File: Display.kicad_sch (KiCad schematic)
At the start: 10 parts, among them J3 541043431, U6 1SS383TE85L_F

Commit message: Create PCB
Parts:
- removed C27: 1uF, Capacitor_SMD:C_0603_1608Metric, symbol Device:C_Small
- added C28: 1uF, Capacitor_SMD:C_0603_1608Metric, symbol Device:C_Small
- added R17: 100K, Resistor_SMD:R_0402_1005Metric, symbol Device:R_Small
- C27: renamed from C26; DigiKey_Part_Number (none) -> 311-1445-1-ND; Manufacturer_Part_Number (none) -> CC0603KRX5R8BB105; Price (none) -> €0.95
- C29: renamed from C28; DigiKey_Part_Number (none) -> 311-1445-1-ND; Manufacturer_Part_Number (none) -> CC0603KRX5R8BB105; Price (none) -> €0.95
- C30: renamed from C29; DigiKey_Part_Number (none) -> 311-1445-1-ND; Manufacturer_Part_Number (none) -> CC0603KRX5R8BB105; Price (none) -> €0.95
- C31: renamed from C30; footprint Capacitor_SMD:C_0603_1608Metric -> Capacitor_SMD:C_0805_2012Metric; DigiKey_Part_Number (none) -> 1276-1244-1-ND; Manufacturer_Part_Number (none) -> CL21A475KAQNNNE; Price (none) -> €0.30
- C32: renamed from C31; footprint Capacitor_SMD:C_0603_1608Metric -> Capacitor_SMD:C_0805_2012Metric; DigiKey_Part_Number (none) -> 1276-1244-1-ND; Manufacturer_Part_Number (none) -> CL21A475KAQNNNE; Price (none) -> €0.30
- J3: DigiKey_Part_Number (none) -> 900-0541043431CT-ND; Manufacturer_Part_Number (none) -> 0541043431; Price (none) -> €2.66
- R18: renamed from R16; value 49.9 -> 100K; footprint Resistor_SMD:R_0603_1608Metric -> Resistor_SMD:R_0402_1005Metric; DigiKey_Part_Number (none) -> 311-100KLRCT-ND; Manufacturer_Part_Number (none) -> RC0402FR-07100KL; Price (none) -> €0.40
- R19: renamed from R17; footprint Resistor_SMD:R_0603_1608Metric -> Resistor_SMD:R_0402_1005Metric; DigiKey_Part_Number (none) -> YAG5649CT-ND; Manufacturer_Part_Number (none) -> AC0402FR-071M2L; Price (none) -> €0.10
- U7: renamed from U6; DigiKey_Part_Number (none) -> 1SS383(TE85LF)CT-ND; Manufacturer_Part_Number (none) -> 1SS383(TE85L,F); Price (none) -> €0.27
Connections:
- net 3V3: now also C27.1, C28.1; no longer C27.2
- net GND: now also C27.2, C28.2; no longer C27.1
- net at J3.7, R18.1: now also R17.1
- net at R18.2, U7.2: now also R17.2
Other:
- moved on the sheet: C27, R18, U7

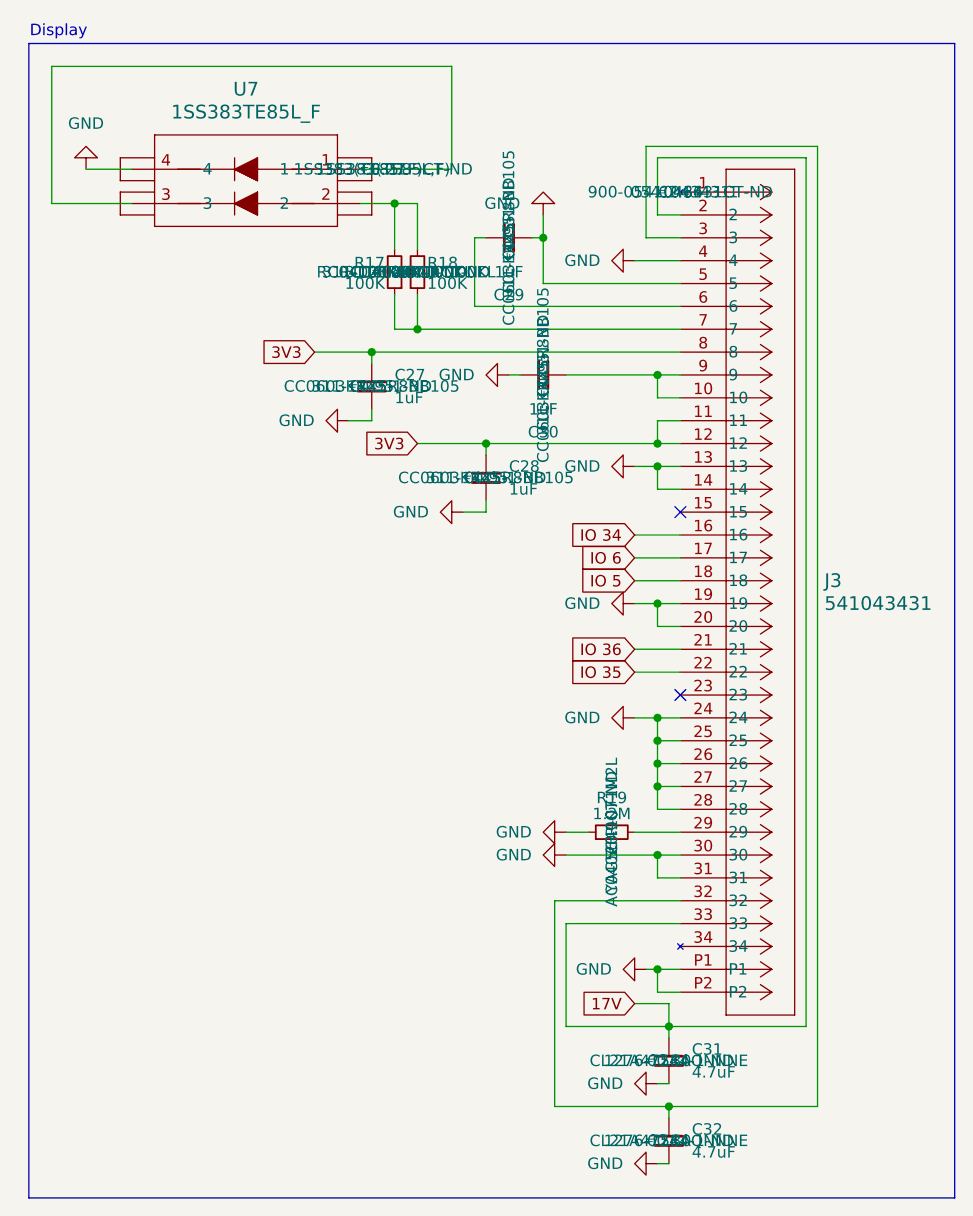
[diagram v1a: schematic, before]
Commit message: Fix minor design mistakes
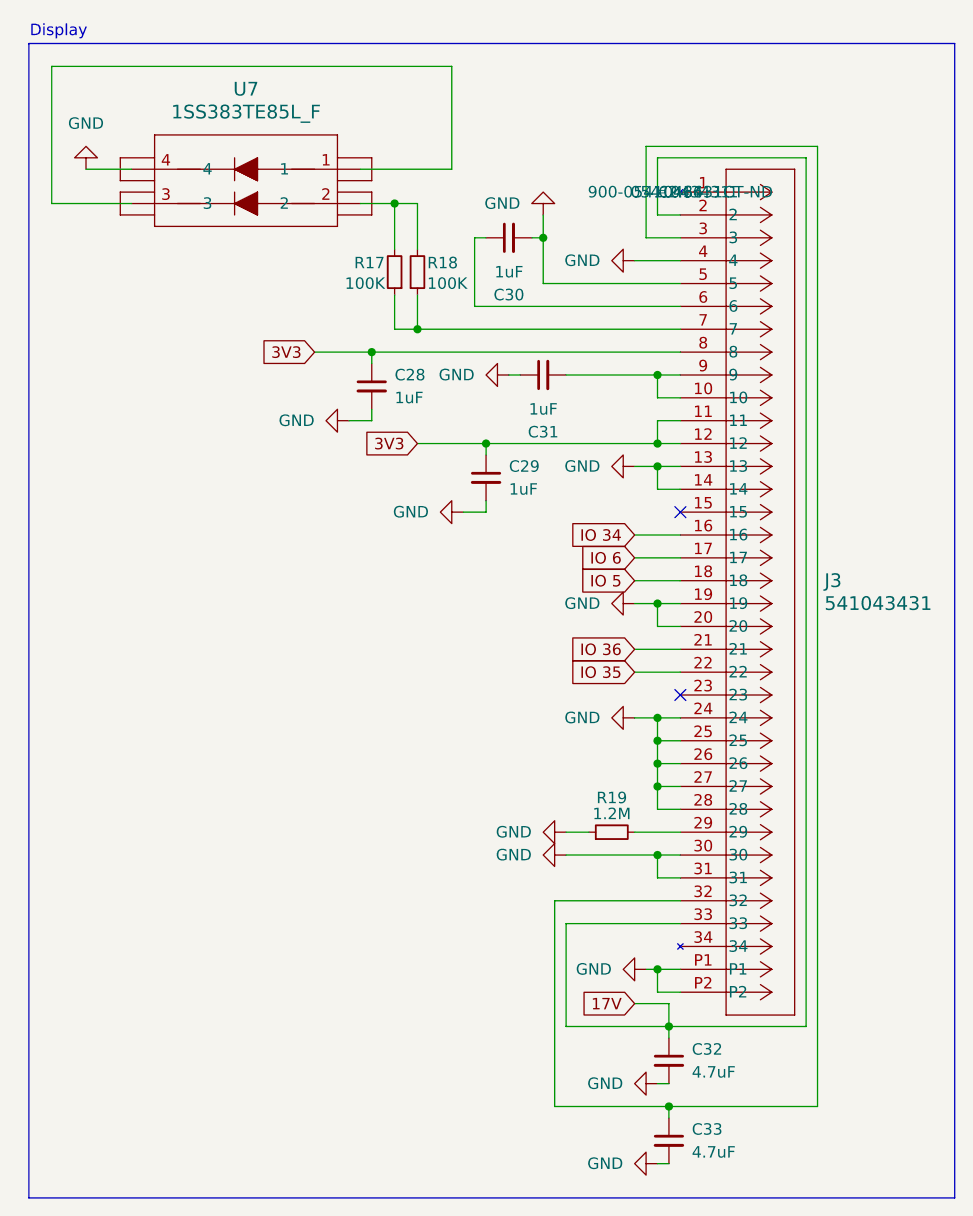
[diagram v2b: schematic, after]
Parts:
- renumbered C27 to C28, C28 to C29, C29 to C30, C30 to C31, C31 to C32, C32 to C33
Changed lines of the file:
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@@
 		(dnp no)
 		(fields_autoplaced yes)
-		(property "Reference" "#PWR032"
+		(property "Reference" "#PWR034"
 			(at 55.88 67.31 0)
 			(effects
@@
 			(project "RFID_Device"
 				(path "/f4733a35-9ae9-40ca-bc69-86dc96557334/b995fd20-39e2-4c72-9eca-13ccf0f092d3"
-					(reference "#PWR032")
+					(reference "#PWR034")
 					(unit 1)
 				)
@@
 					(size 1.27 1.27)
 				)
+				(hide yes)
 			)
 		)
@@
 					(size 1.27 1.27)
 				)
+				(hide yes)
 			)
 		)
@@
 					(size 1.27 1.27)
 				)
+				(hide yes)
 			)
 		)
@@
 		(dnp no)
 		(fields_autoplaced yes)
-		(property "Reference" "#PWR041"
+		(property "Reference" "#PWR043"
 			(at 76.2 118.11 0)
 			(effects
@@
 			(project "RFID_Device"
 				(path "/f4733a35-9ae9-40ca-bc69-86dc96557334/b995fd20-39e2-4c72-9eca-13ccf0f092d3"
-					(reference "#PWR041")
+					(reference "#PWR043")
 					(unit 1)
 				)
@@
 		(dnp no)
 		(fields_autoplaced yes)
-		(property "Reference" "C32"
+		(property "Reference" "C33"
 			(at 87.63 135.8962 0)
 			(effects
@@
 					(size 1.27 1.27)
 				)
+				(hide yes)
 			)
 		)
@@
 					(size 1.27 1.27)
 				)
+				(hide yes)
 			)
 		)
@@
 					(size 1.27 1.27)
 				)
+				(hide yes)
 			)
 		)
@@
 			(project "RFID_Device"
 				(path "/f4733a35-9ae9-40ca-bc69-86dc96557334/b995fd20-39e2-4c72-9eca-13ccf0f092d3"
-					(reference "C32")
+					(reference "C33")
 					(unit 1)
 				)
@@
 		(dnp no)
 		(fields_autoplaced yes)
-		(property "Reference" "#PWR039"
+		(property "Reference" "#PWR041"
 			(at 74.93 77.47 0)
 			(effects
@@
 			(project "RFID_Device"
 				(path "/f4733a35-9ae9-40ca-bc69-86dc96557334/b995fd20-39e2-4c72-9eca-13ccf0f092d3"
-					(reference "#PWR039")
+					(reference "#PWR041")
 					(unit 1)
 				)
@@
 					(size 1.27 1.27)
 				)
+				(hide yes)
 			)
 		)
@@
 					(size 1.27 1.27)
 				)
+				(hide yes)
 			)
 		)
@@
 					(size 1.27 1.27)
 				)
+				(hide yes)
 			)
 		)
@@
 		(dnp no)
 		(fields_autoplaced yes)
-		(property "Reference" "#PWR043"
+		(property "Reference" "#PWR045"
 			(at 77.47 139.7 0)
 			(effects
@@
 			(project "RFID_Device"
 				(path "/f4733a35-9ae9-40ca-bc69-86dc96557334/b995fd20-39e2-4c72-9eca-13ccf0f092d3"
-					(reference "#PWR043")
+					(reference "#PWR045")
 					(unit 1)
 				)
@@
 		(dnp no)
 		(fields_autoplaced yes)
-		(property "Reference" "#PWR037"
+		(property "Reference" "#PWR039"
 			(at 74.93 39.37 0)
 			(effects
@@
 			(project "RFID_Device"
 				(path "/f4733a35-9ae9-40ca-bc69-86dc96557334/b995fd20-39e2-4c72-9eca-13ccf0f092d3"
-					(reference "#PWR037")
+					(reference "#PWR039")
 					(unit 1)
 				)
@@
 					(size 1.27 1.27)
 				)
+				(hide yes)
 			)
 		)
@@
 					(size 1.27 1.27)
 				)
+				(hide yes)
 			)
 		)
@@
 					(size 1.27 1.27)
 				)
+				(hide yes)
 			)
 		)
@@
 		(dnp no)
 		(fields_autoplaced yes)
-		(property "Reference" "#PWR030"
+		(property "Reference" "#PWR032"
 			(at 20.32 22.86 0)
 			(effects
@@
 			(project "RFID_Device"
 				(path "/f4733a35-9ae9-40ca-bc69-86dc96557334/b995fd20-39e2-4c72-9eca-13ccf0f092d3"
-					(reference "#PWR030")
+					(reference "#PWR032")
 					(unit 1)
 				)
@@
 		(dnp no)
 		(fields_autoplaced yes)
-		(property "Reference" "#PWR040"
+		(property "Reference" "#PWR042"
 			(at 74.93 90.17 0)
 			(effects
@@
 			(project "RFID_Device"
 				(path "/f4733a35-9ae9-40ca-bc69-86dc96557334/b995fd20-39e2-4c72-9eca-13ccf0f092d3"
-					(reference "#PWR040")
+					(reference "#PWR042")
 					(unit 1)
 				)
@@
 		(dnp no)
 		(fields_autoplaced yes)
-		(property "Reference" "#PWR038"
+		(property "Reference" "#PWR040"
 			(at 74.93 62.23 0)
 			(effects
@@
 			(project "RFID_Device"
 				(path "/f4733a35-9ae9-40ca-bc69-86dc96557334/b995fd20-39e2-4c72-9eca-13ccf0f092d3"
-					(reference "#PWR038")
+					(reference "#PWR040")
 					(unit 1)
 				)
@@
 		(dnp no)
 		(fields_autoplaced yes)
-		(property "Reference" "#PWR035"
+		(property "Reference" "#PWR037"
 			(at 67.31 102.87 0)
 			(effects
@@
 			(project "RFID_Device"
 				(path "/f4733a35-9ae9-40ca-bc69-86dc96557334/b995fd20-39e2-4c72-9eca-13ccf0f092d3"
-					(reference "#PWR035")
+					(reference "#PWR037")
 					(unit 1)
 				)
@@
 		(on_board yes)
 		(dnp no)
-		(property "Reference" "#PWR034"
+		(property "Reference" "#PWR036"
 			(at 71.12 27.94 0)
 			(effects
@@
 			(project "RFID_Device"
 				(path "/f4733a35-9ae9-40ca-bc69-86dc96557334/b995fd20-39e2-4c72-9eca-13ccf0f092d3"
-					(reference "#PWR034")
+					(reference "#PWR036")
 					(unit 1)
 				)
@@
 		(dnp no)
 		(fields_autoplaced yes)
-		(property "Reference" "#PWR036"
+		(property "Reference" "#PWR038"
 			(at 67.31 105.41 0)
 			(effects
@@
 			(project "RFID_Device"
 				(path "/f4733a35-9ae9-40ca-bc69-86dc96557334/b995fd20-39e2-4c72-9eca-13ccf0f092d3"
-					(reference "#PWR036")
+					(reference "#PWR038")
 					(unit 1)
 				)
@@
 		(dnp no)
 		(fields_autoplaced yes)
-		(property "Reference" "C27"
+		(property "Reference" "C28"
 			(at 54.61 52.0762 0)
 			(effects
@@
 					(size 1.27 1.27)
 				)
+				(hide yes)
 			)
 		)
@@
 					(size 1.27 1.27)
 				)
+				(hide yes)
 			)
 		)
@@
 					(size 1.27 1.27)
 				)
+				(hide yes)
 			)
 		)
@@
 			(project "RFID_Device"
 				(path "/f4733a35-9ae9-40ca-bc69-86dc96557334/b995fd20-39e2-4c72-9eca-13ccf0f092d3"
-					(reference "C27")
+					(reference "C28")
 					(unit 1)
 				)
@@
 		(dnp no)
 		(fields_autoplaced yes)
-		(property "Reference" "#PWR031"
+		(property "Reference" "#PWR033"
 			(at 43.18 57.15 0)
 			(effects
@@
 			(project "RFID_Device"
 				(path "/f4733a35-9ae9-40ca-bc69-86dc96557334/b995fd20-39e2-4c72-9eca-13ccf0f092d3"
-					(reference "#PWR031")
+					(reference "#PWR033")
 					(unit 1)
 				)
@@
 		(dnp no)
 		(fields_autoplaced yes)
-		(property "Reference" "C31"
+		(property "Reference" "C32"
 			(at 87.63 127.0062 0)
 			(effects
@@
 					(size 1.27 1.27)
 				)
+				(hide yes)
 			)
 		)
@@
 					(size 1.27 1.27)
 				)
+				(hide yes)
 			)
 		)
@@
 					(size 1.27 1.27)
 				)
+				(hide yes)
 			)
 		)
@@
 			(project "RFID_Device"
 				(path "/f4733a35-9ae9-40ca-bc69-86dc96557334/b995fd20-39e2-4c72-9eca-13ccf0f092d3"
-					(reference "C31")
+					(reference "C32")
 					(unit 1)
 				)
@@
 		(on_board yes)
 		(dnp no)
-		(property "Reference" "C29"
+		(property "Reference" "C30"
 			(at 67.3163 43.18 90)
 			(effects
@@
 					(size 1.27 1.27)
 				)
+				(hide yes)
 			)
 		)
@@
 					(size 1.27 1.27)
 				)
+				(hide yes)
 			)
 		)
@@
 					(size 1.27 1.27)
 				)
+				(hide yes)
 			)
 		)
@@
 			(project "RFID_Device"
 				(path "/f4733a35-9ae9-40ca-bc69-86dc96557334/b995fd20-39e2-4c72-9eca-13ccf0f092d3"
-					(reference "C29")
+					(reference "C30")
 					(unit 1)
 				)
@@
 		(dnp no)
 		(fields_autoplaced yes)
-		(property "Reference" "C28"
+		(property "Reference" "C29"
 			(at 67.31 62.2362 0)
 			(effects
@@
 					(size 1.27 1.27)
 				)
+				(hide yes)
 			)
 		)
@@
 					(size 1.27 1.27)
 				)
+				(hide yes)
 			)
 		)
@@
 					(size 1.27 1.27)
 				)
+				(hide yes)
 			)
 		)
@@
 			(project "RFID_Device"
 				(path "/f4733a35-9ae9-40ca-bc69-86dc96557334/b995fd20-39e2-4c72-9eca-13ccf0f092d3"
-					(reference "C28")
+					(reference "C29")
 					(unit 1)
 				)
@@
 		(dnp no)
 		(fields_autoplaced yes)
-		(property "Reference" "#PWR033"
+		(property "Reference" "#PWR035"
 			(at 60.96 52.07 0)
 			(effects
@@
 			(project "RFID_Device"
 				(path "/f4733a35-9ae9-40ca-bc69-86dc96557334/b995fd20-39e2-4c72-9eca-13ccf0f092d3"
-					(reference "#PWR033")
+					(reference "#PWR035")
 					(unit 1)
 				)
@@
 					(size 1.27 1.27)
 				)
+				(hide yes)
 			)
 		)
@@
 					(size 1.27 1.27)
 				)
+				(hide yes)
 			)
 		)
@@
 					(size 1.27 1.27)
 				)
+				(hide yes)
 			)
 		)
@@
 		(dnp no)
 		(fields_autoplaced yes)
-		(property "Reference" "#PWR042"
+		(property "Reference" "#PWR044"
 			(at 77.47 130.81 0)
 			(effects
@@
 			(project "RFID_Device"
 				(path "/f4733a35-9ae9-40ca-bc69-86dc96557334/b995fd20-39e2-4c72-9eca-13ccf0f092d3"
-					(reference "#PWR042")
+					(reference "#PWR044")
 					(unit 1)
 				)
@@
 		(on_board yes)
 		(dnp no)
-		(property "Reference" "C30"
+		(property "Reference" "C31"
 			(at 71.1263 58.42 90)
 			(effects
@@
 					(size 1.27 1.27)
 				)
+				(hide yes)
 			)
 		)
@@
 					(size 1.27 1.27)
 				)
+				(hide yes)
 			)
 		)
@@
 					(size 1.27 1.27)
 				)
+				(hide yes)
 			)
 		)
@@
 			(project "RFID_Device"
 				(path "/f4733a35-9ae9-40ca-bc69-86dc96557334/b995fd20-39e2-4c72-9eca-13ccf0f092d3"
-					(reference "C30")
-					(unit 1)
-				)
+					(reference "C31")
+					(unit 1)
+				)
